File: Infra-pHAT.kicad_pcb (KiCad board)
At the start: 2 copper layers, 65 x 30 mm, 24 parts, among them Q1 BC817, U1 CAT24C32WI-GT3

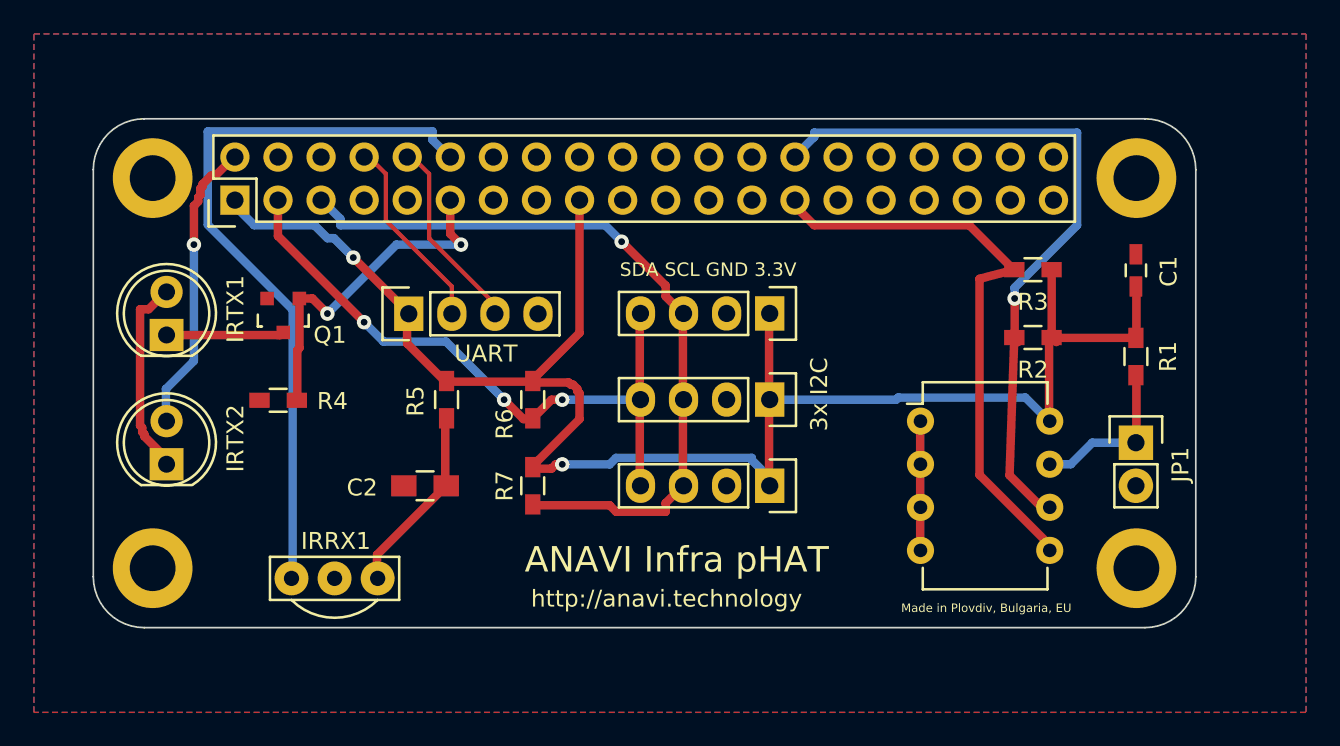
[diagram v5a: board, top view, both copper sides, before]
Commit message: Add logo and update tesxt on the silkscreen
Signed-off-by: Leon Anavi <leon@anavi.org>
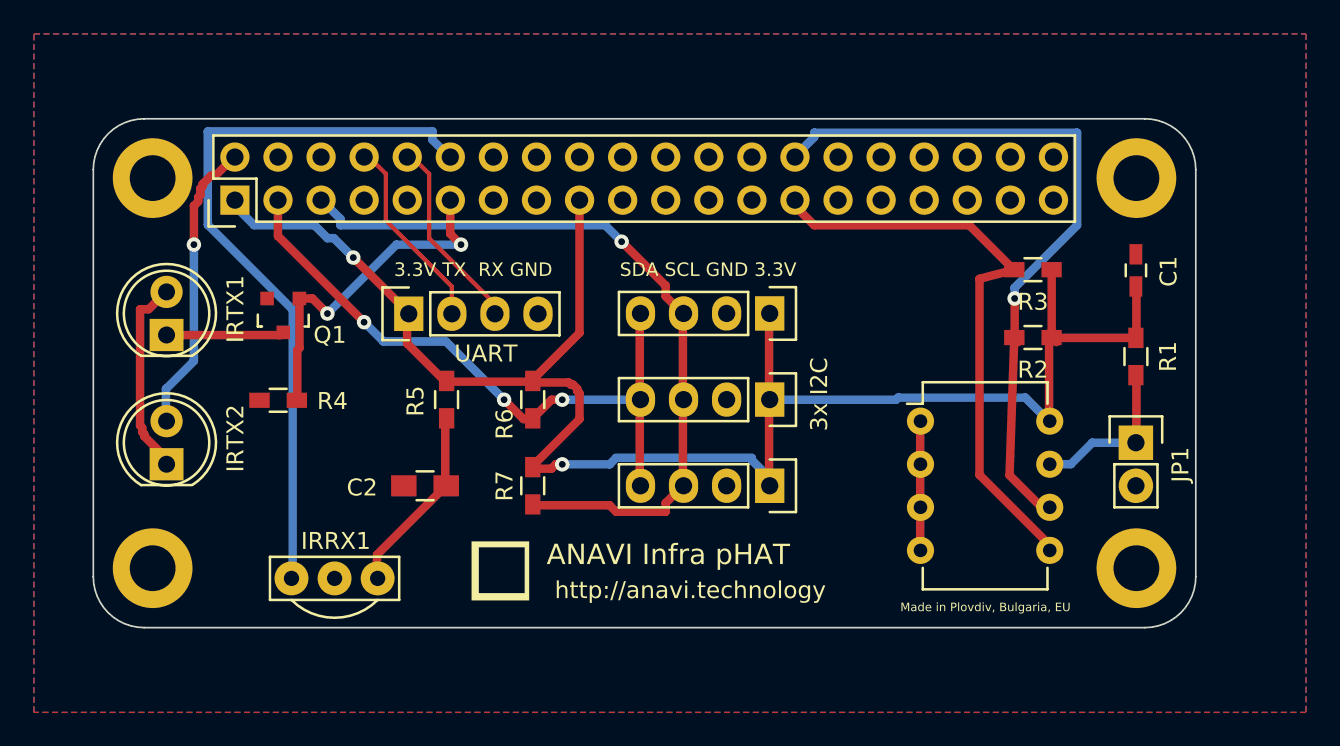
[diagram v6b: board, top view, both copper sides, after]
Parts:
- added ?: LOGO, logo:anavi-logo, F.Cu at (172.5, 101.7)
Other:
- board text added: "3.3V TX RX GND"
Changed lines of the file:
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@@
     (area 148.451099 74.953599 213.551101 105.053601)
     (thickness 1.6)
-    (drawings 20)
+    (drawings 21)
     (tracks 236)
     (zones 0)
-    (modules 24)
+    (modules 25)
     (nets 36)
   )
@@
     (pad 4 thru_hole circle (at 0 0) (size 4.7 4.7) (drill 2.7) (layers *.Cu *.Mask F.SilkS))
   )
+  (module logo:anavi-logo (layer F.Cu)
+    (at 172.5 101.7)
+    (fp_text reference "" (at 0 0) (layer F.SilkS) hide
+      (effects (font (thickness 0.3)))
+    )
+    (fp_text value LOGO (at 0.75 0) (layer F.SilkS) hide
+      (effects (font (thickness 0.3)))
+    )
+    (fp_poly (pts (xy 1.693334 1.693334) (xy -1.693333 1.693334) (xy -1.693333 -1.439333) (xy -1.27 -1.439333)
+      (xy -1.27 1.27) (xy 1.439334 1.27) (xy 1.439334 -1.439333) (xy -1.27 -1.439333)
+      (xy -1.693333 -1.439333) (xy -1.693333 -1.778) (xy 1.693334 -1.778) (xy 1.693334 1.693334)) (layer F.SilkS) (width 0.01))
+  )
+  (gr_text "3.3V TX  RX GND" (at 170.9 83.9) (layer F.SilkS)
+    (effects (font (size 0.8 0.8) (thickness 0.125)))
+  )
   (gr_text "3x I2C" (at 191.3 91.25 90) (layer F.SilkS)
     (effects (font (size 1 1) (thickness 0.25)))
@@
     (effects (font (size 0.8 0.8) (thickness 0.125)))
   )
-  (gr_text "Made in Plovdiv, Bulgaria, EU" (at 201.15 103.85) (layer F.SilkS)
+  (gr_text "Made in Plovdiv, Bulgaria, EU" (at 201.1 103.8) (layer F.SilkS)
     (effects (font (size 0.5 0.5) (thickness 0.125)))
   )
-  (gr_text http://anavi.technology (at 182.3 103.3) (layer F.SilkS)
-    (effects (font (size 1 1) (thickness 0.25)))
-  )
-  (gr_text "ANAVI Infra pHAT" (at 182.9 101) (layer F.SilkS)
-    (effects (font (size 1.5 1.5) (thickness 0.3)))
+  (gr_text http://anavi.technology (at 183.7 102.8) (layer F.SilkS)
+    (effects (font (size 1 1) (thickness 0.2)))
+  )
+  (gr_text "ANAVI Infra pHAT" (at 182.4 100.7) (layer F.SilkS)
+    (effects (font (size 1.2 1.2) (thickness 0.3)))
   )
   (dimension 3.5 (width 0.3) (layer F.CrtYd)

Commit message: Infra-pHAT.kicad_pcb: Add revision number
Signed-off-by: Leon Anavi <leon@anavi.org>
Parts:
- moved ? 2.80 mm to (175.3, 101.7)
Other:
- board text added: "Rev 1.0 (c) 2017"
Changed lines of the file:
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@@
     (links 59)
     (no_connects 2)
-    (area 148.451099 74.953599 213.551101 105.053601)
+    (area 136.817429 66.3 225.182572 110.000001)
     (thickness 1.6)
-    (drawings 21)
+    (drawings 22)
     (tracks 236)
     (zones 0)
@@
     (pcbplotparams
       (layerselection 0x00030_80000001)
-      (usegerberextensions false)
+      (usegerberextensions true)
       (excludeedgelayer true)
       (linewidth 0.100000)
@@
       (outputformat 1)
       (mirror false)
-      (drillshape 1)
+      (drillshape 0)
       (scaleselection 1)
-      (outputdirectory ""))
+      (outputdirectory plots/))
   )
   (net 0 "")
@@
   )
   (module logo:anavi-logo (layer F.Cu)
-    (at 172.5 101.7)
+    (at 175.3 101.7)
     (fp_text reference "" (at 0 0) (layer F.SilkS) hide
       (effects (font (thickness 0.3)))
@@
       (xy -1.693333 -1.439333) (xy -1.693333 -1.778) (xy 1.693334 -1.778) (xy 1.693334 1.693334)) (layer F.SilkS) (width 0.01))
   )
+  (gr_text "Rev 1.0 (c) 2017" (at 181.5 101.9) (layer F.SilkS)
+    (effects (font (size 0.6 0.6) (thickness 0.15)))
+  )
   (gr_text "3.3V TX  RX GND" (at 170.9 83.9) (layer F.SilkS)
     (effects (font (size 0.8 0.8) (thickness 0.125)))
@@
     (effects (font (size 0.5 0.5) (thickness 0.125)))
   )
-  (gr_text http://anavi.technology (at 183.7 102.8) (layer F.SilkS)
-    (effects (font (size 1 1) (thickness 0.2)))
-  )
-  (gr_text "ANAVI Infra pHAT" (at 182.4 100.7) (layer F.SilkS)
-    (effects (font (size 1.2 1.2) (thickness 0.3)))
+  (gr_text http://anavi.technology (at 182.9 102.9) (layer F.SilkS)
+    (effects (font (size 0.6 0.6) (thickness 0.15)))
+  )
+  (gr_text "ANAVI Infra pHAT" (at 183.9 100.7) (layer F.SilkS)
+    (effects (font (size 1 1) (thickness 0.25)))
   )
   (dimension 3.5 (width 0.3) (layer F.CrtYd)
